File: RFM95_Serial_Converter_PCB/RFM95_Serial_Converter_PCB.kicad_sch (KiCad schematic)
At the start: 16 parts

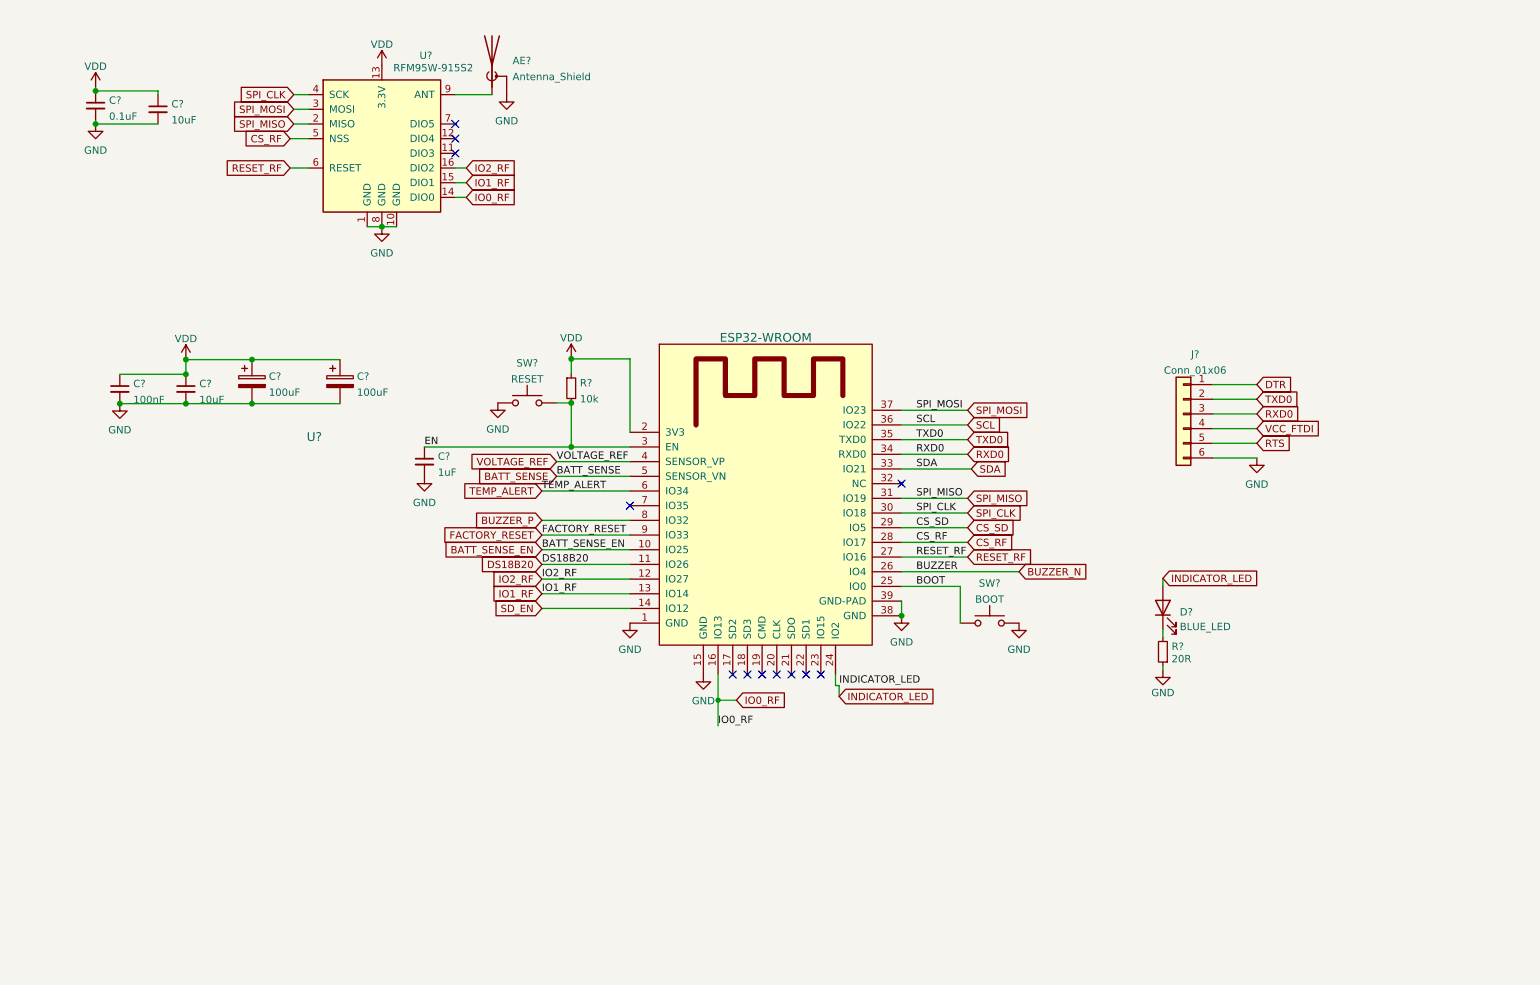
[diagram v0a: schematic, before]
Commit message: Swapped to stm32F405
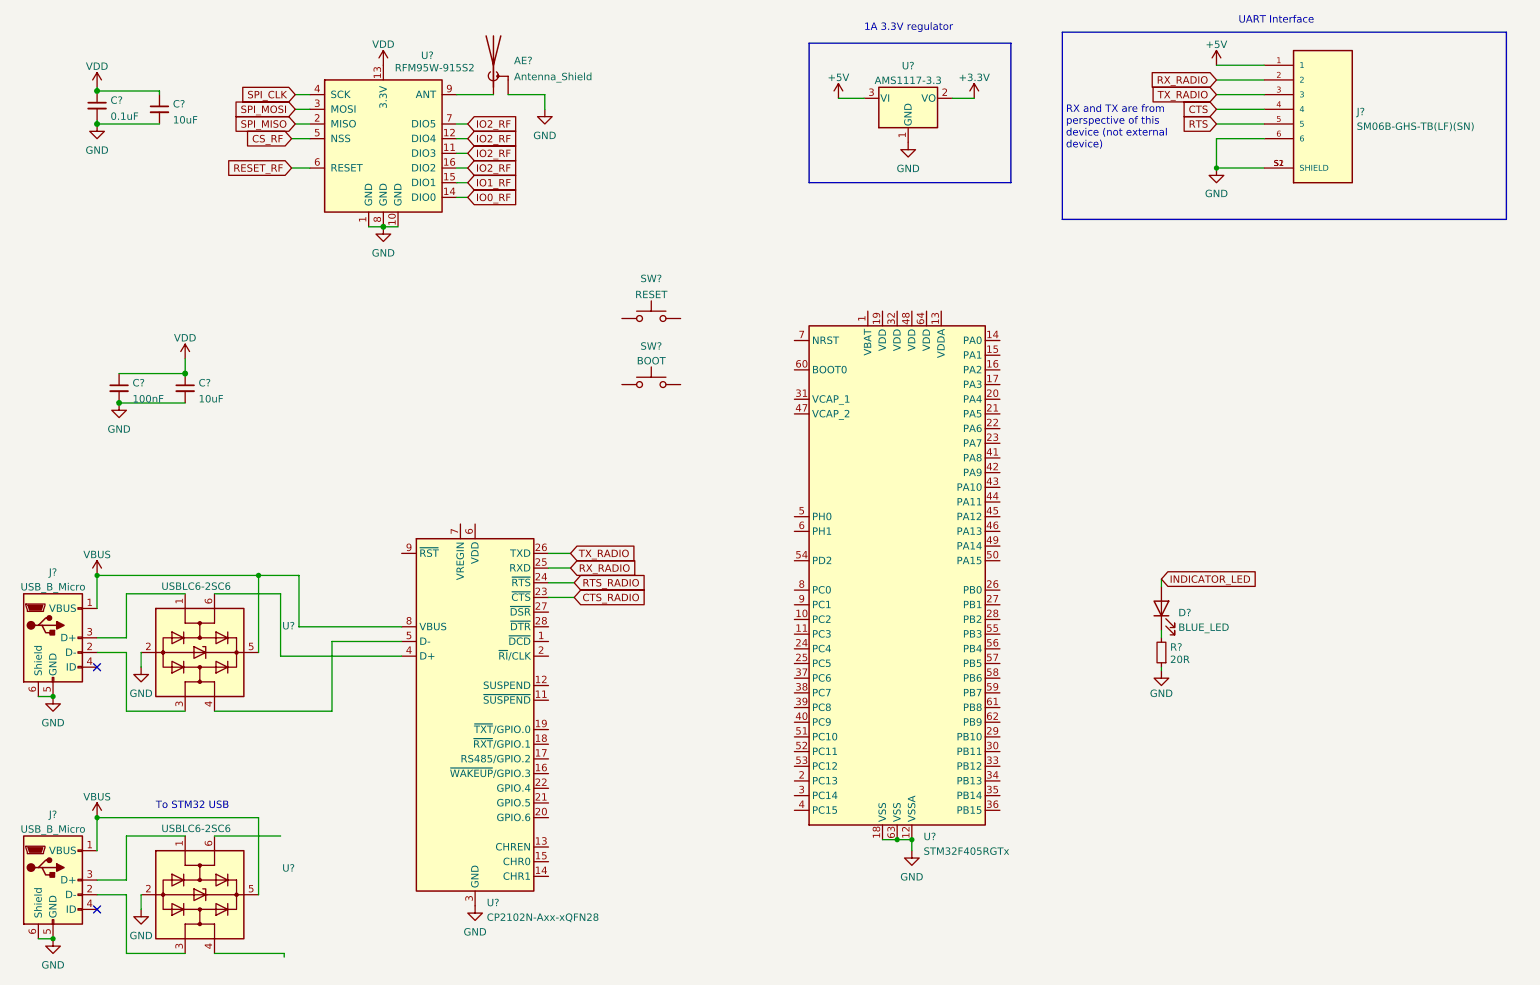
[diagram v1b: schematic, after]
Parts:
- removed C? (x2): 100uF, Capacitor_Tantalum_SMD:CP_EIA-3528-21_Kemet-B, symbol Device:C_Polarized
- removed C?: 1uF, Capacitor_SMD:C_0603_1608Metric, symbol Device:C_Small
- removed J?: Conn_01x06, Connector_PinHeader_2.54mm:PinHeader_1x06_P2.54mm_Vertical, symbol Connector_Generic:Conn_01x06
- removed R?: 10k, Resistor_SMD:R_0603_1608Metric, symbol Device:R_Small
- removed SW?: RESET, Button_Switch_SMD:SW_Push_1P1T_NO_CK_KSC6xxJ, symbol Switch:SW_Push
- removed SW?: BOOT, Button_Switch_SMD:SW_Push_1P1T_NO_CK_KSC6xxJ, symbol Switch:SW_Push
- removed U?: ESP32-WROOM, RF_Module:ESP32-WROOM-32, symbol ESP32-footprints-Shem-Lib:ESP32-WROOM
- added J?: SM06B-GHS-TB(LF)(SN), JST_SM06B-GHS-TB(LF)(SN), symbol SM06B-GHS-TB_LF__SN_:SM06B-GHS-TB(LF)(SN)
- added J? (x2): USB_B_Micro, symbol Connector:USB_B_Micro
- added SW?: RESET, Button_Switch_SMD:SW_Push_1P1T_NO_CK_KSC6xxJ, symbol Switch:SW_Push
- added SW?: BOOT, Button_Switch_SMD:SW_Push_1P1T_NO_CK_KSC6xxJ, symbol Switch:SW_Push
- added U?: AMS1117-3.3, Package_TO_SOT_SMD:SOT-223-3_TabPin2, symbol Regulator_Linear:AMS1117-3.3
- added U?: STM32F405RGTx, Package_QFP:LQFP-64_10x10mm_P0.5mm, symbol MCU_ST_STM32F4:STM32F405RGTx
- added U?: CP2102N-Axx-xQFN28, Package_DFN_QFN:QFN-28-1EP_5x5mm_P0.5mm_EP3.35x3.35mm, symbol Interface_USB:CP2102N-Axx-xQFN28
- added U? (x2): USBLC6-2SC6, Package_TO_SOT_SMD:SOT-23-6, symbol Power_Protection:USBLC6-2SC6
- AE?: footprint Connector_Coaxial:SMA_Amphenol_132134_Vertical -> Connector_Coaxial:SMA_Amphenol_132289_EdgeMount
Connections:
- net GND: now also J?.5 (GND), J?.5 (GND), J?.6, J?.6 (Shield), J?.6 (Shield), J?.S1 (SHIELD), J?.S2 (SHIELD), U?.1 (GND), U?.12 (VSSA), U?.18 (VSS), U?.2 (GND), U?.2 (GND), U?.29 (GND), U?.3 (GND), U?.63 (VSS)
- net IO2_RF: now also U?.11 (DIO3), U?.12 (DIO4), U?.7 (DIO5)
- net RTS: now also J?.5
- new net: J?.2 (D-), U?.3 (I/O2) (x2)
- new net: J?.3 (D+), U?.1 (I/O1) (x2)
- new net: U?.4 (D+), U?.6 (I/O1)
- new net: U?.4 (I/O2), U?.5 (D-)
- new net +3V3: U?.2 (VO)
- new net +5V: J?.1, U?.3 (VI)
- new net CTS: J?.4
- new net CTS_RADIO: U?.23 (~{CTS})
- new net RTS_RADIO: U?.24 (~{RTS})
- new net RX_RADIO: J?.2, U?.25 (RXD)
- new net TX_RADIO: J?.3, U?.26 (TXD)
- new net VBUS: J?.1 (VBUS), J?.1 (VBUS), U?.5 (VBUS), U?.5 (VBUS), U?.8 (VBUS)
- no-connect marks 12 -> 2
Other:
- note added: "1A 3.3V regulator"
- note added: "RX and TX are from perspective of this device (not external device)"
- note added: "To STM32 USB"
- note added: "UART Interface"

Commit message: Schematic almost finished
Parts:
- removed SW?: RESET, Button_Switch_SMD:SW_Push_1P1T_NO_CK_KSC6xxJ, symbol Switch:SW_Push
- removed SW?: BOOT, Button_Switch_SMD:SW_Push_1P1T_NO_CK_KSC6xxJ, symbol Switch:SW_Push
- added C?: 0.1uF, Capacitor_SMD:C_0805_2012Metric_Pad1.15x1.40mm_HandSolder, symbol Nebula-rescue:C_Small-Device-H7_FlightComputer-rescue
- added C?: 1u, Capacitor_SMD:C_0603_1608Metric, symbol Device:C_Small
- added C? (x2): 2.2u, Capacitor_SMD:C_0603_1608Metric, symbol Device:C_Small
- added C? (x2): 10nF, Capacitor_SMD:C_0603_1608Metric, symbol Device:C_Small
- added H? (x4): MountingHole, MountingHole:MountingHole_2.5mm_Pad, symbol Mechanical:MountingHole
- added J?: SM06B-GHS-TB(LF)(SN), JST_SM06B-GHS-TB(LF)(SN), symbol SM06B-GHS-TB_LF__SN_:SM06B-GHS-TB(LF)(SN)
- added J?: Conn_01x04, Connector_PinHeader_2.54mm:PinHeader_1x04_P2.54mm_Horizontal, symbol Connector_Generic:Conn_01x04
- added R? (x2): 10R, Resistor_SMD:R_0805_2012Metric_Pad1.15x1.40mm_HandSolder, symbol Nebula-rescue:R_Small-Device-H7_FlightComputer-rescue
- added R? (x2): 10k, Resistor_SMD:R_0805_2012Metric_Pad1.15x1.40mm_HandSolder, symbol Nebula-rescue:R_Small-Device-H7_FlightComputer-rescue
- added SW? (x2): SW_Push, Button_Switch_SMD:SW_Push_1P1T_NO_CK_KSC6xxJ, symbol Nebula-rescue:SW_Push-Switch-H7_FlightComputer-rescue
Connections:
- net CTS is gone; now on net CTS_RADIO: J?.4
- net RTS is gone; now on net RTS_RADIO: J?.5
- net VDD is gone; now on net +3V3: C?.1, C?.1, C?.1, C?.1, U?.13 (3.3V)
- net +3V3: now also U?.19 (VDD), U?.32 (VDD), U?.48 (VDD), U?.6 (VDD), U?.64 (VDD), U?.7 (VREGIN), C?.1, C?.1, C?.1, J?.1, J?.1 (Pin_1), R?.2, SW?.1
- net CS_RF: now also U?.20 (PA4)
- net CTS_RADIO: now also U?.24 (~{RTS}), U?.44 (PA11); no longer U?.23 (~{CTS})
- net GND: now also C?.1, C?.2, C?.2, C?.2, C?.2, C?.2, J?.4 (Pin_4), J?.6, J?.S1 (SHIELD), J?.S2 (SHIELD), R?.1, SW?.1
- net IO0_RF: now also U?.27 (PB1)
- net IO1_RF: now also U?.29 (PB10)
- net IO2_RF: now also U?.30 (PB11); no longer U?.11 (DIO3), U?.12 (DIO4), U?.7 (DIO5)
- net RESET_RF: now also U?.26 (PB0)
- net RTS_RADIO: now also U?.23 (~{CTS}), U?.45 (PA12); no longer U?.24 (~{RTS})
- net RX_RADIO: now also U?.43 (PA10)
- net SPI_CLK: now also U?.21 (PA5)
- net SPI_MISO: now also U?.22 (PA6)
- net SPI_MOSI: now also U?.23 (PA7)
- net TX_RADIO: now also U?.42 (PA9)
- net CTS_2: now reaches U?.14 (PA0)
- net CTS_2: now also J?.4
- net RTS_2: now reaches U?.15 (PA1)
- net RTS_2: now also J?.5
- net TX_2: now reaches U?.16 (PA2)
- net TX_2: now also J?.3
- net RX_2: now reaches U?.17 (PA3)
- net RX_2: now also J?.2
- net OSC32_IN: now reaches U?.3 (PC14)
- net at U?.31 (VCAP_1): now also C?.1
- net IO3_RF: now reaches U?.33 (PB12)
- net IO3_RF: now also U?.11 (DIO3)
- net IO4_RF: now reaches U?.34 (PB13)
- net IO4_RF: now also U?.12 (DIO4)
- net at U?.35 (PB14): now also R?.2
- net at U?.36 (PB15): now also R?.2
- net OSC32_OUT: now reaches U?.4 (PC15)
- net IO5_RF: now reaches U?.41 (PA8)
- net IO5_RF: now also U?.7 (DIO5)
- net SWDIO: now reaches U?.46 (PA13)
- net SWDIO: now also J?.2 (Pin_2)
- net at U?.47 (VCAP_2): now also C?.1
- net SWCLK: now reaches U?.49 (PA14)
- net SWCLK: now also J?.3 (Pin_3)
- net OSC_IN: now reaches U?.5 (PH0)
- net OSC_OUT: now reaches U?.6 (PH1)
- net at U?.60 (BOOT0): now also R?.2, SW?.2
- net at U?.7 (NRST): now also C?.2, SW?.2
- net at U?.9 (~{RST}): now also R?.1
- net USB_D-: now reaches U?.4 (I/O2)
- net USB_D-: now also R?.1
- net USB_D+: now reaches U?.6 (I/O1)
- net USB_D+: now also R?.1
- no-connect marks 2 -> 19
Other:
- note added: "External UART2 Interface"
- note added: "Radio UART1 Interface"
- note added: "SWD Programming Interface"
- note added: "https://lcsc.com/products/Oscillators_364.html"
- note removed: "UART Interface"
- moved on the sheet: D?, R?

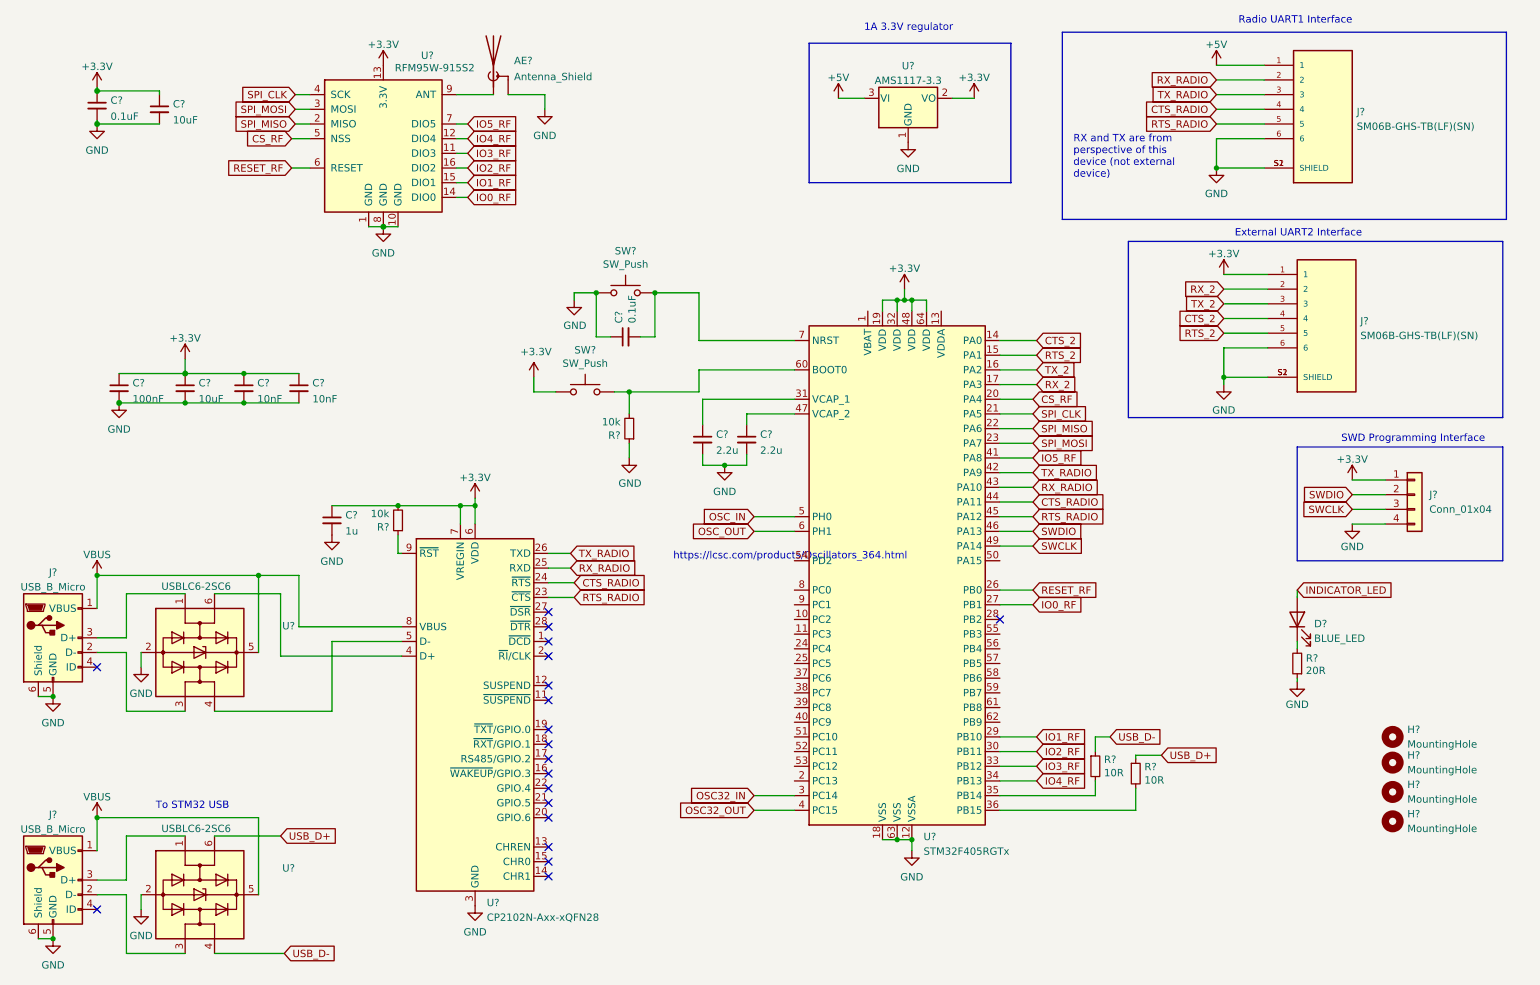
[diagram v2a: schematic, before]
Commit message: Started component placement
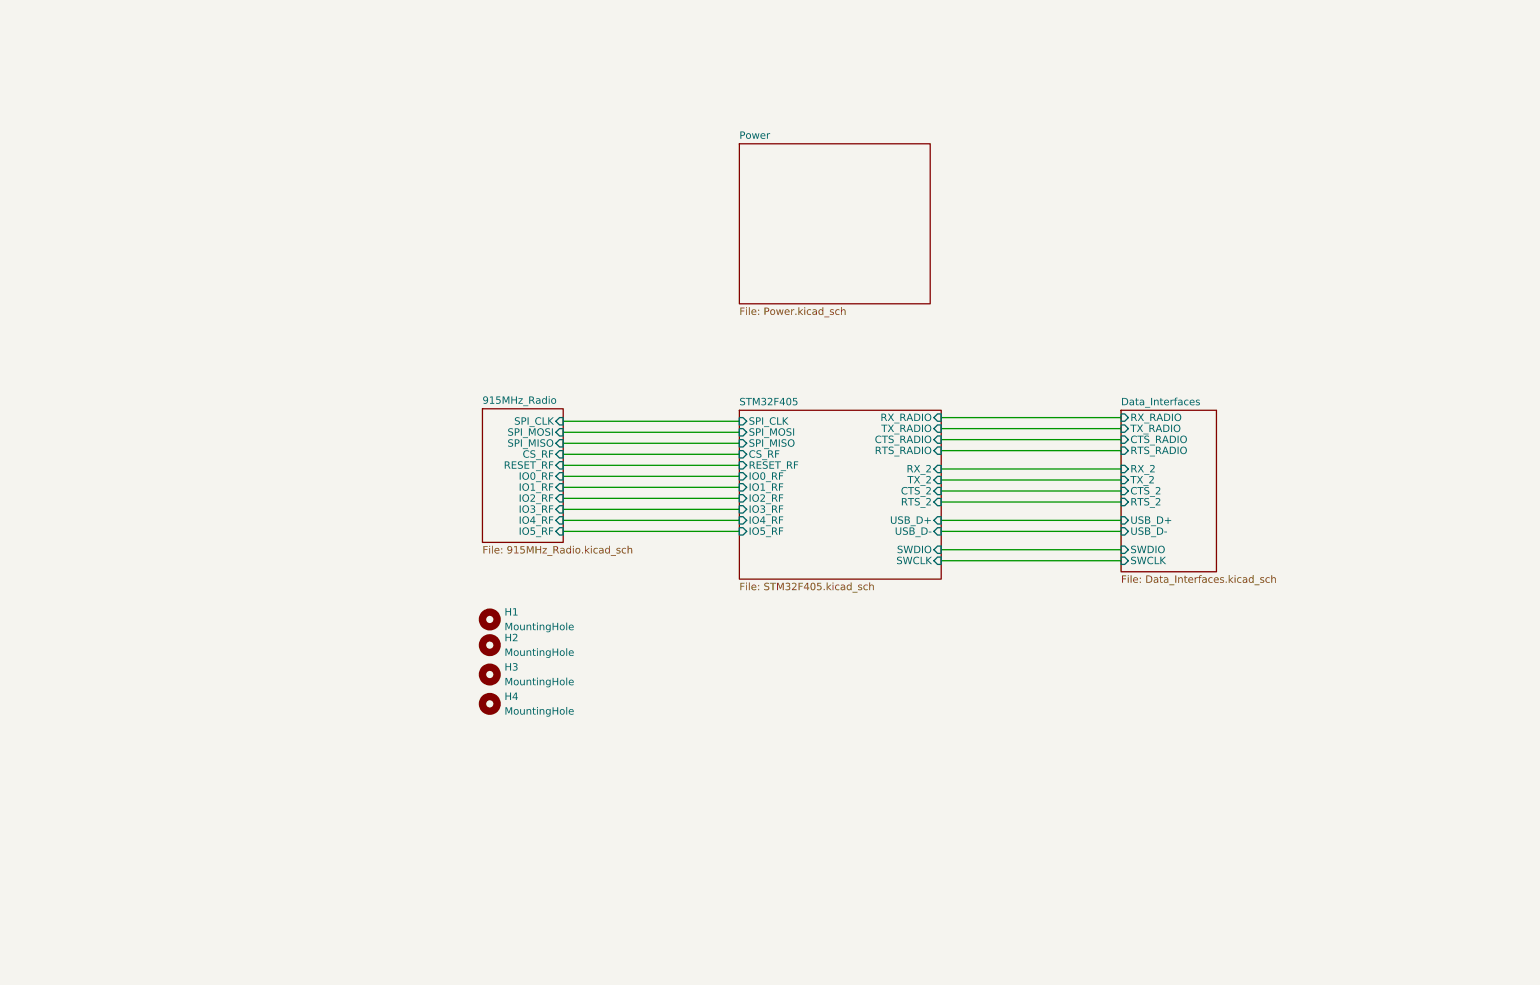
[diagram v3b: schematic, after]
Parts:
- removed AE?: Antenna_Shield, Connector_Coaxial:SMA_Amphenol_132289_EdgeMount, symbol Device:Antenna_Shield
- removed C?: 0.1uF, Capacitor_SMD:C_0805_2012Metric_Pad1.15x1.40mm_HandSolder, symbol Nebula-rescue:C_Small-Device-H7_FlightComputer-rescue
- removed C?: 1u, Capacitor_SMD:C_0603_1608Metric, symbol Device:C_Small
- removed C? (x2): 10uF, Capacitor_SMD:C_0603_1608Metric, symbol Device:C_Small
- removed C? (x2): 2.2u, Capacitor_SMD:C_0603_1608Metric, symbol Device:C_Small
- removed C?: 0.1uF, Capacitor_SMD:C_0603_1608Metric, symbol Device:C_Small
- removed C? (x2): 10nF, Capacitor_SMD:C_0603_1608Metric, symbol Device:C_Small
- removed C?: 100nF, Capacitor_SMD:C_0603_1608Metric, symbol Device:C_Small
- removed D?: BLUE_LED, LED_SMD:LED_0603_1608Metric_Pad1.05x0.95mm_HandSolder, symbol Device:LED
- removed J? (x2): SM06B-GHS-TB(LF)(SN), JST_SM06B-GHS-TB(LF)(SN), symbol SM06B-GHS-TB_LF__SN_:SM06B-GHS-TB(LF)(SN)
- removed J?: Conn_01x04, Connector_PinHeader_2.54mm:PinHeader_1x04_P2.54mm_Horizontal, symbol Connector_Generic:Conn_01x04
- removed J? (x2): USB_B_Micro, symbol Connector:USB_B_Micro
- removed R? (x2): 10R, Resistor_SMD:R_0805_2012Metric_Pad1.15x1.40mm_HandSolder, symbol Nebula-rescue:R_Small-Device-H7_FlightComputer-rescue
- removed R? (x2): 10k, Resistor_SMD:R_0805_2012Metric_Pad1.15x1.40mm_HandSolder, symbol Nebula-rescue:R_Small-Device-H7_FlightComputer-rescue
- removed R?: 20R, Resistor_SMD:R_0603_1608Metric, symbol Device:R_Small
- removed SW? (x2): SW_Push, Button_Switch_SMD:SW_Push_1P1T_NO_CK_KSC6xxJ, symbol Nebula-rescue:SW_Push-Switch-H7_FlightComputer-rescue
- removed U?: AMS1117-3.3, Package_TO_SOT_SMD:SOT-223-3_TabPin2, symbol Regulator_Linear:AMS1117-3.3
- removed U?: STM32F405RGTx, Package_QFP:LQFP-64_10x10mm_P0.5mm, symbol MCU_ST_STM32F4:STM32F405RGTx
- removed U?: CP2102N-Axx-xQFN28, Package_DFN_QFN:QFN-28-1EP_5x5mm_P0.5mm_EP3.35x3.35mm, symbol Interface_USB:CP2102N-Axx-xQFN28
- removed U?: RFM95W-915S2, RF_Module:HOPERF_RFM9XW_SMD, symbol RF_Module:RFM95W-915S2
- removed U? (x2): USBLC6-2SC6, Package_TO_SOT_SMD:SOT-23-6, symbol Power_Protection:USBLC6-2SC6
- gave numbers to parts that had none: 4
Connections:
- no-connect marks 19 -> 0
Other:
- added sheet 915MHz_Radio (915MHz_Radio.kicad_sch)
- added sheet Data_Interfaces (Data_Interfaces.kicad_sch)
- added sheet Power (Power.kicad_sch)
- added sheet STM32F405 (STM32F405.kicad_sch)
- note removed: "1A 3.3V regulator"
- note removed: "External UART2 Interface"
- note removed: "RX and TX are from perspective of this device (not external device)"
- note removed: "Radio UART1 Interface"
- note removed: "SWD Programming Interface"
- note removed: "To STM32 USB"
- note removed: "https://lcsc.com/products/Oscillators_364.html"
- moved on the sheet: H1, H2, H3, H4
